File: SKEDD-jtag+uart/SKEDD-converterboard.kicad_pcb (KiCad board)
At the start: 2 copper layers, 22.9 x 16.5 mm, 7 parts, among them J1 Conn_ARM_JTAG_SWD_10, J2 uart_client_2.54, J3 swd_with_uart_client, J4 Conn_01x02_Male

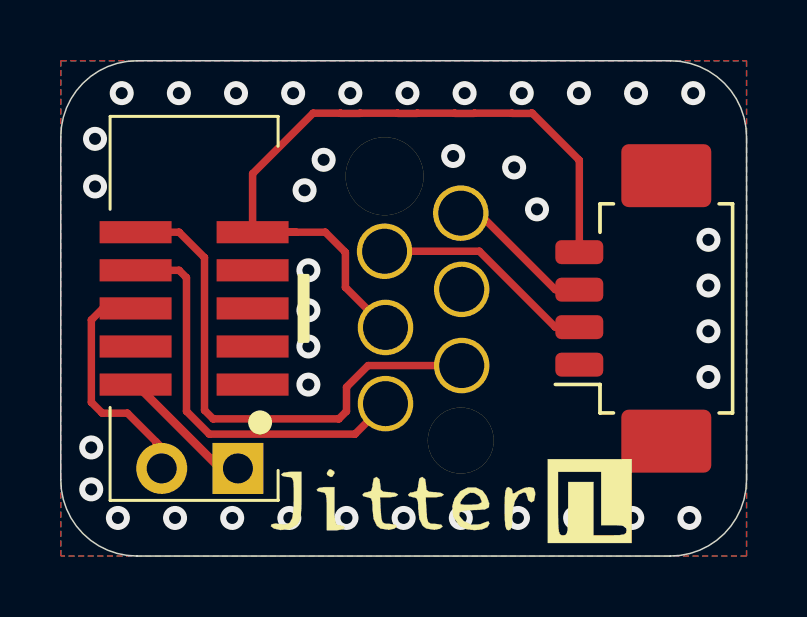
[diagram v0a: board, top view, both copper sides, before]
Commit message: SKED-jtag+uart, jtag-swd: add MPN info, BOM
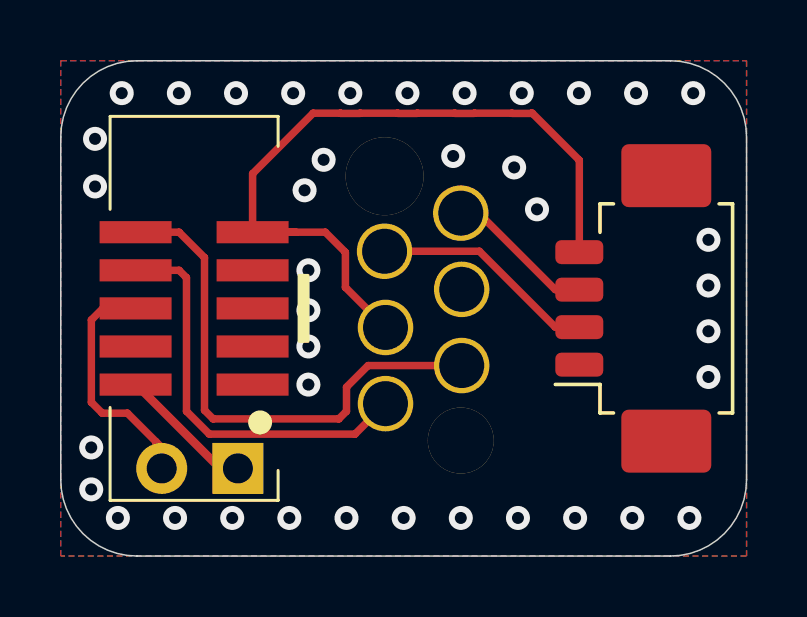
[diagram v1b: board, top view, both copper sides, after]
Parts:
- removed G*** (x2): LOGO, Jitter_Logos:Jitter-mini
- removed REF**: JitterLogo, Jitter_Logos:JitterLogo
- J3: value swd_with_uart_client -> DNI
- J4: value Conn_01x02_Male -> DNI
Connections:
- J1 pad 7: Net-(J1-Pad7) -> (no net)
- J1 pad 8: Net-(J1-Pad8) -> (no net)
- J2 pad MP: GND -> (no net)
